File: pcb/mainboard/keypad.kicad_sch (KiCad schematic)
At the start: 7 parts, among them J801 Conn_02x20_Odd_Even_MountingP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, J802 Conn_02x10_Odd_Even_MountingP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, U801 74LS154

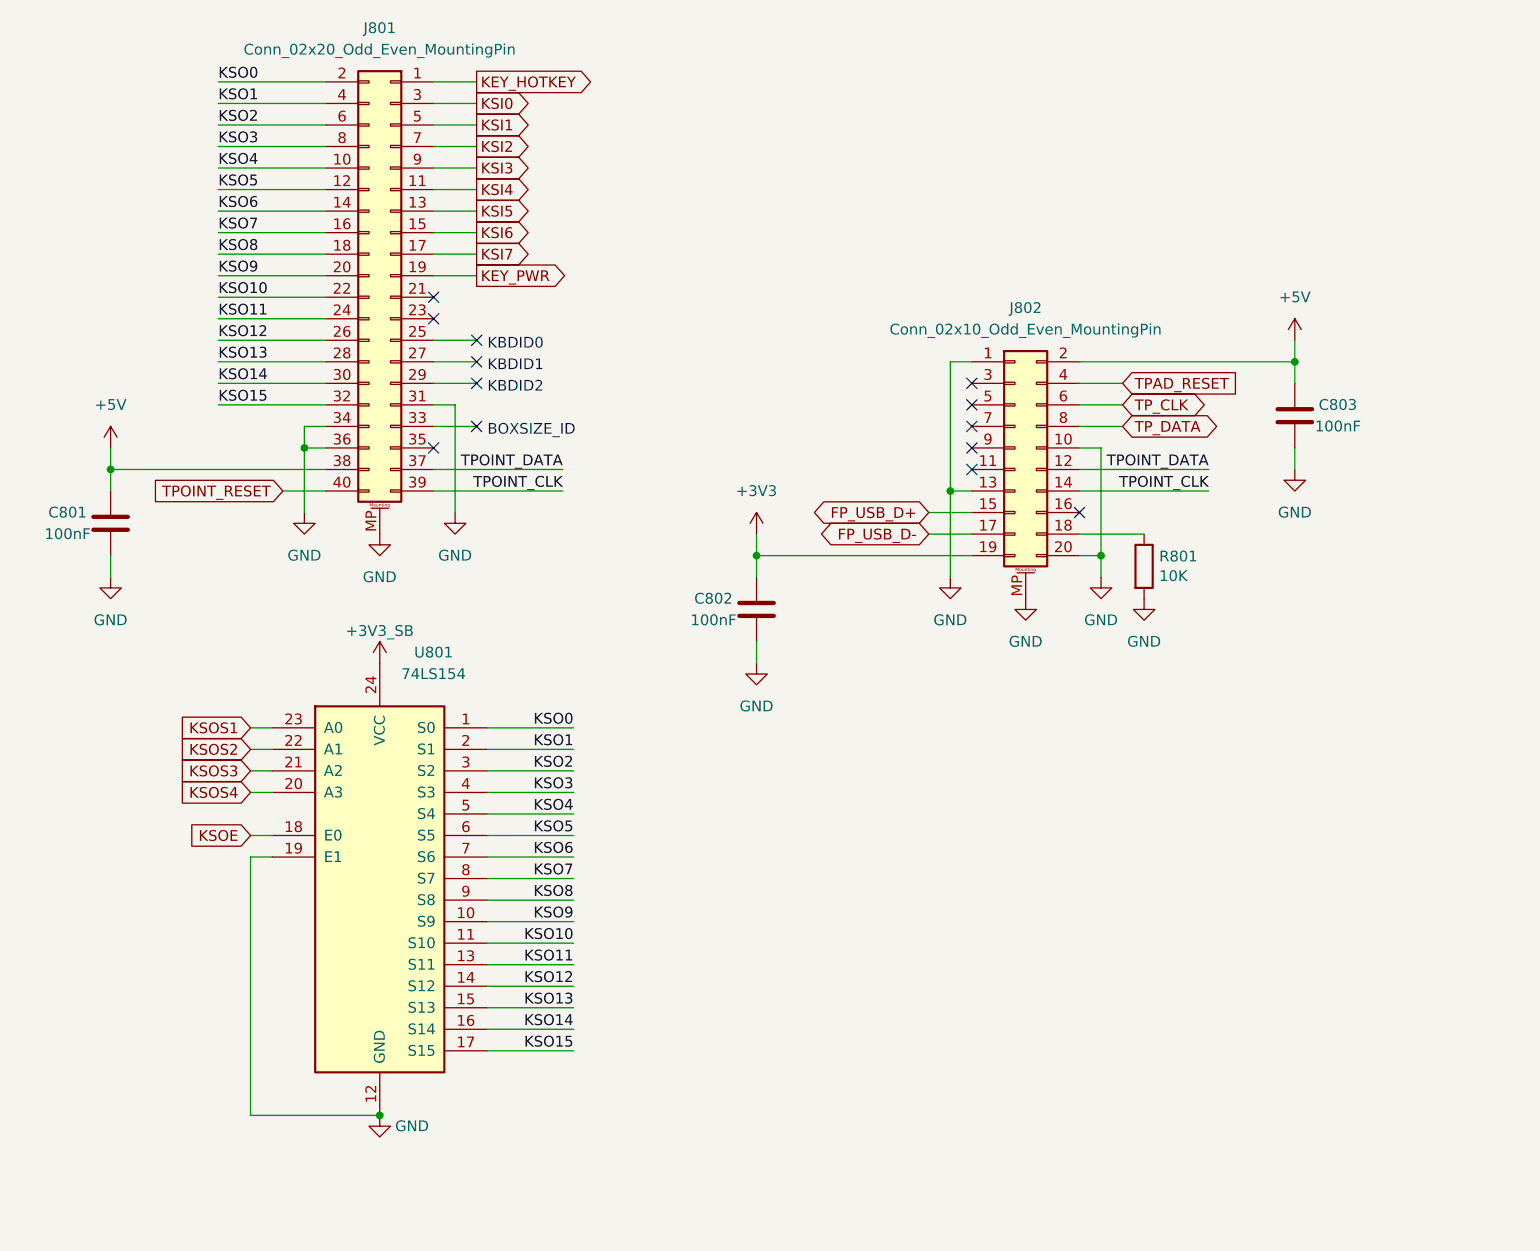
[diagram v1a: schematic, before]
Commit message: pcb: initial placement for mb
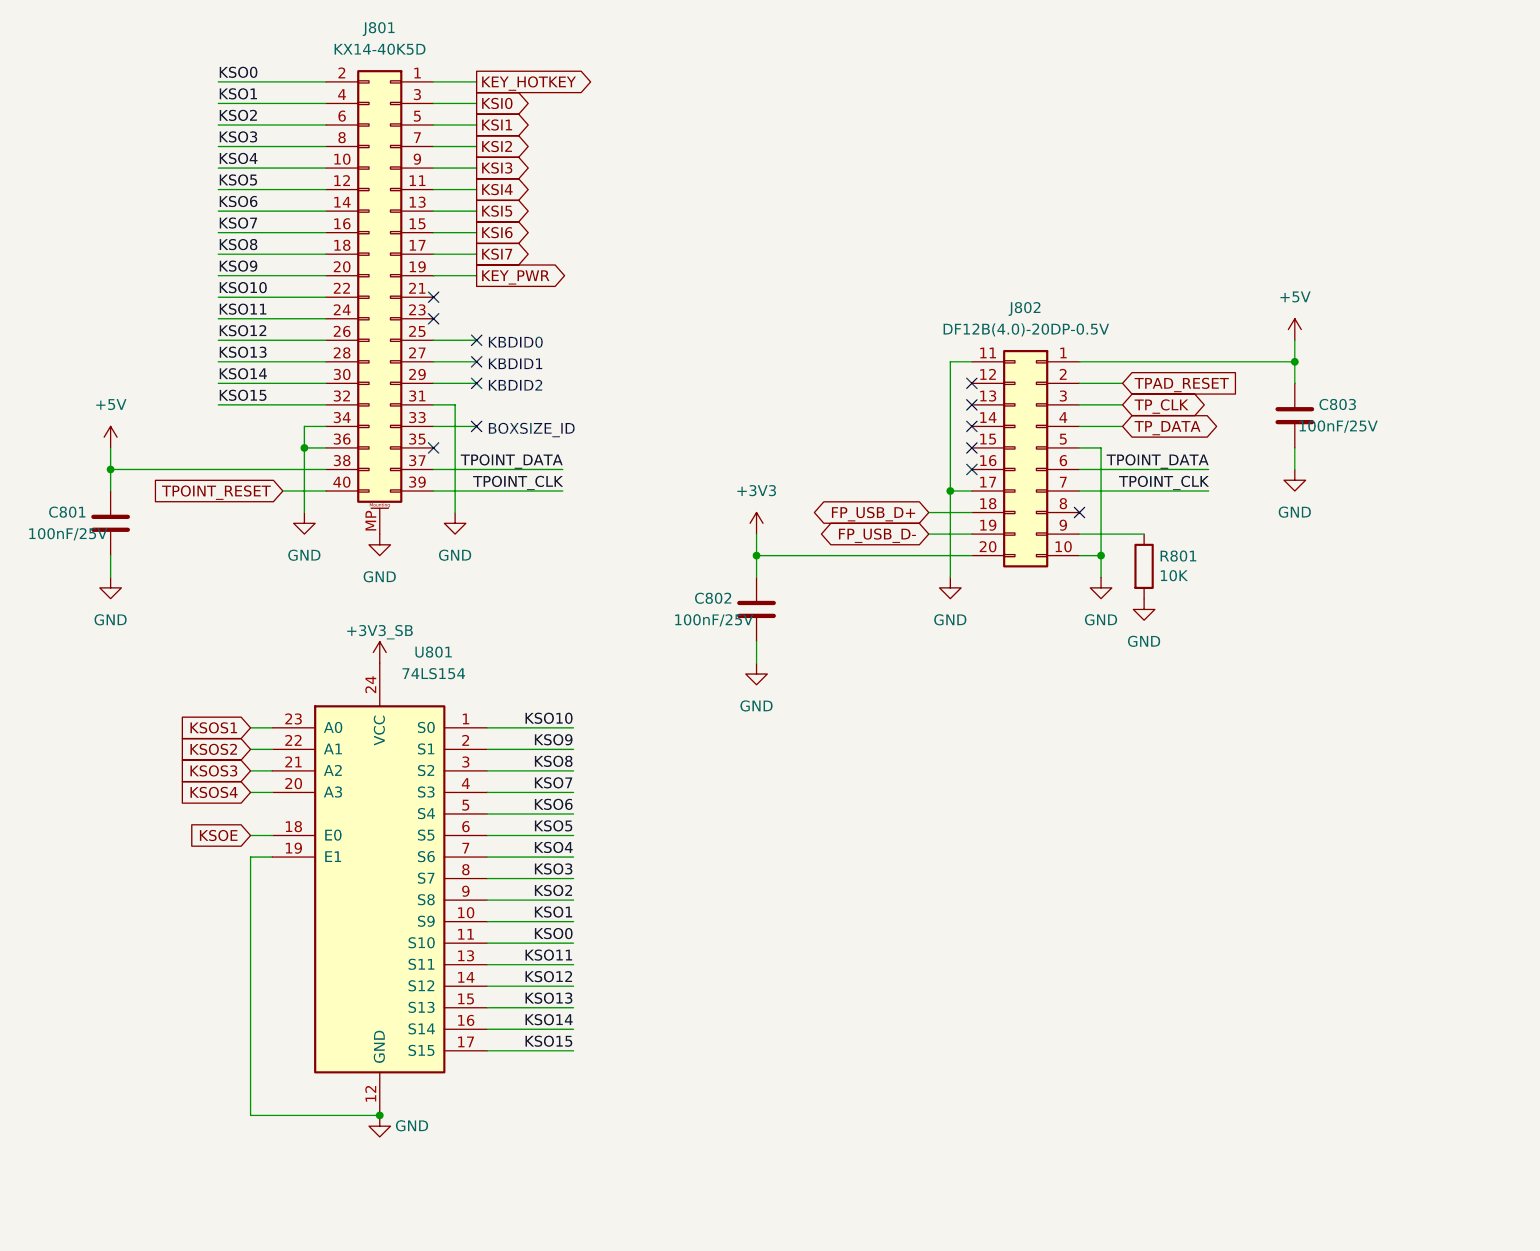
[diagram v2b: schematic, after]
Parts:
- removed J802: Conn_02x10_Odd_Even_MountingPin, Connector_Hirose:Hirose_DF12_DF12E3.0-20DP-0.5V_2x10_P0.50mm_Vertical, symbol Connector_Generic_MountingPin:Conn_02x10_Odd_Even_MountingPin
- added J802: DF12B(4.0)-20DP-0.5V, Connector_Hirose:Hirose_DF12_DF12E3.0-20DP-0.5V_2x10_P0.50mm_Vertical, symbol Connector_Generic:Conn_02x10_Top_Bottom
- C801, C802, C803: value 100nF -> 100nF/25V; LCSC (none) -> C56392; Ref.Price (none) -> 0.0023
- J801: value Conn_02x20_Odd_Even_MountingPin -> KX14-40K5D; Ref.Price (none) -> 3.75
- R801: LCSC (none) -> C60489; Ref.Price (none) -> 0.0006
- U801: LCSC (none) -> C21061; Ref.Price (none) -> 0.4058
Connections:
- net +3V3: now also J802.20 (Pin_20)
- net +5V: now also J802.1 (Pin_1)
- net FP_USB_D+: now also J802.18 (Pin_18)
- net FP_USB_D-: now also J802.19 (Pin_19)
- net GND: now also J802.10 (Pin_10), J802.11 (Pin_11), J802.17 (Pin_17), J802.5 (Pin_5)
- net KSO0: now also U801.11 (S10); no longer U801.1 (S0)
- net KSO1: now also U801.10 (S9); no longer U801.2 (S1)
- net KSO10: now also U801.1 (S0); no longer U801.11 (S10)
- net KSO2: now also U801.9 (S8); no longer U801.3 (S2)
- net KSO3: now also U801.8 (S7); no longer U801.4 (S3)
- net KSO4: now also U801.7 (S6); no longer U801.5 (S4)
- net KSO6: now also U801.5 (S4); no longer U801.7 (S6)
- net KSO7: now also U801.4 (S3); no longer U801.8 (S7)
- net KSO8: now also U801.3 (S2); no longer U801.9 (S8)
- net KSO9: now also U801.2 (S1); no longer U801.10 (S9)
- net TPAD_RESET: now also J802.2 (Pin_2)
- net TPOINT_CLK: now also J802.7 (Pin_7)
- net TPOINT_DATA: now also J802.6 (Pin_6)
- net TP_CLK: now also J802.3 (Pin_3)
- net TP_DATA: now also J802.4 (Pin_4)
- net at R801.1: now also J802.9 (Pin_9)
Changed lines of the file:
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@@
     (effects (font (size 1.27 1.27)) (justify right bottom))
   )
-  (label "KSO0" (at 128.27 121.92 180)
-    (effects (font (size 1.27 1.27)) (justify right bottom))
-  )
-  (label "KSO1" (at 128.27 124.46 180)
-    (effects (font (size 1.27 1.27)) (justify right bottom))
-  )
-  (label "KSO2" (at 128.27 127 180)
-    (effects (font (size 1.27 1.27)) (justify right bottom))
-  )
-  (label "KSO3" (at 128.27 129.54 180)
-    (effects (font (size 1.27 1.27)) (justify right bottom))
-  )
-  (label "KSO4" (at 128.27 132.08 180)
+  (label "KSO10" (at 128.27 121.92 180)
+    (effects (font (size 1.27 1.27)) (justify right bottom))
+  )
+  (label "KSO9" (at 128.27 124.46 180)
+    (effects (font (size 1.27 1.27)) (justify right bottom))
+  )
+  (label "KSO8" (at 128.27 127 180)
+    (effects (font (size 1.27 1.27)) (justify right bottom))
+  )
+  (label "KSO7" (at 128.27 129.54 180)
+    (effects (font (size 1.27 1.27)) (justify right bottom))
+  )
+  (label "KSO6" (at 128.27 132.08 180)
     (effects (font (size 1.27 1.27)) (justify right bottom))
   )
@@
     (effects (font (size 1.27 1.27)) (justify right bottom))
   )
-  (label "KSO6" (at 128.27 137.16 180)
-    (effects (font (size 1.27 1.27)) (justify right bottom))
-  )
-  (label "KSO7" (at 128.27 139.7 180)
-    (effects (font (size 1.27 1.27)) (justify right bottom))
-  )
-  (label "KSO8" (at 128.27 142.24 180)
-    (effects (font (size 1.27 1.27)) (justify right bottom))
-  )
-  (label "KSO9" (at 128.27 144.78 180)
-    (effects (font (size 1.27 1.27)) (justify right bottom))
-  )
-  (label "KSO10" (at 128.27 147.32 180)
+  (label "KSO4" (at 128.27 137.16 180)
+    (effects (font (size 1.27 1.27)) (justify right bottom))
+  )
+  (label "KSO3" (at 128.27 139.7 180)
+    (effects (font (size 1.27 1.27)) (justify right bottom))
+  )
+  (label "KSO2" (at 128.27 142.24 180)
+    (effects (font (size 1.27 1.27)) (justify right bottom))
+  )
+  (label "KSO1" (at 128.27 144.78 180)
+    (effects (font (size 1.27 1.27)) (justify right bottom))
+  )
+  (label "KSO0" (at 128.27 147.32 180)
     (effects (font (size 1.27 1.27)) (justify right bottom))
   )
@@
     )
     (property "Datasheet" "" (id 3) (at 172.72 104.14 0)
-      (effects (font (size 1.27 1.27)) hide)
-    )
-    (pin "1")
-  )
-  (symbol (lib_id "power:GND") (at 181.61 106.68 0) (unit 1)
-    (in_bom yes) (on_board yes) (fields_autoplaced)
-    (property "Reference" "#PWR0811" (id 0) (at 181.61 113.03 0)
-      (effects (font (size 1.27 1.27)) hide)
-    )
-    (property "Value" "GND" (id 1) (at 181.61 111.76 0))
-    (property "Footprint" "" (id 2) (at 181.61 106.68 0)
-      (effects (font (size 1.27 1.27)) hide)
-    )
-    (property "Datasheet" "" (id 3) (at 181.61 106.68 0)
       (effects (font (size 1.27 1.27)) hide)
     )
@@
       (effects (font (size 1.27 1.27)) hide)
     )
+    (property "LCSC" "C60489" (id 4) (at 195.58 102.87 0)
+      (effects (font (size 1.27 1.27)) hide)
+    )
+    (property "Ref.Price" "0.0006" (id 5) (at 195.58 102.87 0)
+      (effects (font (size 1.27 1.27)) hide)
+    )
     (pin "1")
     (pin "2")
@@
     (in_bom yes) (on_board yes)
     (property "Reference" "C801" (id 0) (at 68.58 96.52 0))
-    (property "Value" "100nF" (id 1) (at 68.58 99.06 0))
+    (property "Value" "100nF/25V" (id 1) (at 68.58 99.06 0))
     (property "Footprint" "Capacitor_SMD:C_0402_1005Metric" (id 2) (at 74.6252 93.98 0)
       (effects (font (size 1.27 1.27)) hide)
     )
     (property "Datasheet" "~" (id 3) (at 73.66 97.79 0)
+      (effects (font (size 1.27 1.27)) hide)
+    )
+    (property "LCSC" "C56392" (id 4) (at 73.66 97.79 0)
+      (effects (font (size 1.27 1.27)) hide)
+    )
+    (property "Ref.Price" "0.0023" (id 5) (at 73.66 97.79 0)
       (effects (font (size 1.27 1.27)) hide)
     )
@@
     (in_bom yes) (on_board yes)
     (property "Reference" "C802" (id 0) (at 144.78 106.68 0))
-    (property "Value" "100nF" (id 1) (at 144.78 109.22 0))
+    (property "Value" "100nF/25V" (id 1) (at 144.78 109.22 0))
     (property "Footprint" "Capacitor_SMD:C_0402_1005Metric" (id 2) (at 150.8252 104.14 0)
       (effects (font (size 1.27 1.27)) hide)
     )
     (property "Datasheet" "~" (id 3) (at 149.86 107.95 0)
+      (effects (font (size 1.27 1.27)) hide)
+    )
+    (property "LCSC" "C56392" (id 4) (at 149.86 107.95 0)
+      (effects (font (size 1.27 1.27)) hide)
+    )
+    (property "Ref.Price" "0.0023" (id 5) (at 149.86 107.95 0)
       (effects (font (size 1.27 1.27)) hide)
     )
@@
     (in_bom yes) (on_board yes)
     (property "Reference" "C803" (id 0) (at 218.44 83.82 0))
-    (property "Value" "100nF" (id 1) (at 218.44 86.36 0))
+    (property "Value" "100nF/25V" (id 1) (at 218.44 86.36 0))
     (property "Footprint" "Capacitor_SMD:C_0402_1005Metric" (id 2) (at 212.3948 81.28 0)
       (effects (font (size 1.27 1.27)) hide)
@@
       (effects (font (size 1.27 1.27)) hide)
     )
+    (property "LCSC" "C56392" (id 4) (at 213.36 85.09 0)
+      (effects (font (size 1.27 1.27)) hide)
+    )
+    (property "Ref.Price" "0.0023" (id 5) (at 213.36 85.09 0)
+      (effects (font (size 1.27 1.27)) hide)
+    )
     (pin "1")
     (pin "2")
   )
-  (symbol (lib_id "Connector_Generic_MountingPin:Conn_02x10_Odd_Even_MountingPin") (at 180.34 88.9 0) (unit 1)
+  (symbol (lib_id "Connector_Generic:Conn_02x10_Top_Bottom") (at 182.88 88.9 0) (mirror y) (unit 1)
     (in_bom yes) (on_board yes) (fields_autoplaced)
     (property "Reference" "J802" (id 0) (at 181.61 72.39 0))
-    (property "Value" "Conn_02x10_Odd_Even_MountingPin" (id 1) (at 181.61 74.93 0))
-    (property "Footprint" "Connector_Hirose:Hirose_DF12_DF12E3.0-20DP-0.5V_2x10_P0.50mm_Vertical" (id 2) (at 180.34 88.9 0)
-      (effects (font (size 1.27 1.27)) hide)
-    )
-    (property "Datasheet" "~" (id 3) (at 180.34 88.9 0)
+    (property "Value" "DF12B(4.0)-20DP-0.5V" (id 1) (at 181.61 74.93 0))
+    (property "Footprint" "Connector_Hirose:Hirose_DF12_DF12E3.0-20DP-0.5V_2x10_P0.50mm_Vertical" (id 2) (at 182.88 88.9 0)
+      (effects (font (size 1.27 1.27)) hide)
+    )
+    (property "Datasheet" "~" (id 3) (at 182.88 88.9 0)
+      (effects (font (size 1.27 1.27)) hide)
+    )
+    (property "LCSC" "H11727CT-ND" (id 4) (at 182.88 88.9 0)
+      (effects (font (size 1.27 1.27)) hide)
+    )
+    (property "Ref.Price" "1.02" (id 5) (at 182.88 88.9 0)
       (effects (font (size 1.27 1.27)) hide)
     )
@@
     (pin "8")
     (pin "9")
-    (pin "MP")
   )
   (symbol (lib_id "Connector_Generic_MountingPin:Conn_02x20_Odd_Even_MountingPin") (at 106.68 68.58 0) (mirror y) (unit 1)
     (in_bom yes) (on_board yes) (fields_autoplaced)
     (property "Reference" "J801" (id 0) (at 105.41 39.37 0))
-    (property "Value" "Conn_02x20_Odd_Even_MountingPin" (id 1) (at 105.41 41.91 0))
+    (property "Value" "KX14-40K5D" (id 1) (at 105.41 41.91 0))
     (property "Footprint" "footprints:JAE_KX14-40K5D" (id 2) (at 106.68 68.58 0)
       (effects (font (size 1.27 1.27)) hide)
     )
     (property "Datasheet" "~" (id 3) (at 106.68 68.58 0)
+      (effects (font (size 1.27 1.27)) hide)
+    )
+    (property "Ref.Price" "3.75" (id 4) (at 106.68 68.58 0)
       (effects (font (size 1.27 1.27)) hide)
     )
@@
       (effects (font (size 1.27 1.27)) hide)
     )
+    (property "LCSC" "C21061" (id 4) (at 105.41 139.7 0)
+      (effects (font (size 1.27 1.27)) hide)
+    )
+    (property "Ref.Price" "0.4058" (id 5) (at 105.41 139.7 0)
+      (effects (font (size 1.27 1.27)) hide)
+    )

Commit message: pcb: r0.1 mb routing done
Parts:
- removed J802: DF12B(4.0)-20DP-0.5V, Connector_Hirose:Hirose_DF12_DF12E3.0-20DP-0.5V_2x10_P0.50mm_Vertical, symbol Connector_Generic:Conn_02x10_Top_Bottom
- removed R801: 10K, Resistor_SMD:R_0402_1005Metric, symbol Device:R
- added J802: Conn_01x24_MountingPin, Connector_FFC-FPC:Hirose_FH12-24S-0.5SH_1x24-1MP_P0.50mm_Horizontal, symbol Connector_Generic_MountingPin:Conn_01x24_MountingPin
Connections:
- net +3V3: now also J802.1 (Pin_1), J802.2 (Pin_2)
- net +5V: now also J802.3 (Pin_3), J802.4 (Pin_4)
- net FP_USB_D+: now also J802.6 (Pin_6)
- net FP_USB_D-: now also J802.7 (Pin_7)
- net GND: now also J802.12 (Pin_12), J802.17 (Pin_17), J802.5 (Pin_5), J802.8 (Pin_8), J802.MP (MountPin)
- new net SPK_LN: J802.14 (Pin_14)
- new net SPK_LP: J802.13 (Pin_13)
- new net SPK_RN: J802.16 (Pin_16)
- new net SPK_RP: J802.15 (Pin_15)
- new net TPAD_CLK: J802.10 (Pin_10)
- new net TPAD_DATA: J802.11 (Pin_11)
- no-connect marks 13 -> 8
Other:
- moved on the sheet: C802, C803
